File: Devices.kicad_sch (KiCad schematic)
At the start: 0 parts

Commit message: USB and PWR sch
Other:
- title: (none) -> Devices
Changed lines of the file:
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@@
 	(generator_version "8.0")
 	(paper "A4")
+	(title_block
+		(title "Devices")
+	)
 	(sheet
 		(at 20.32 39.37)

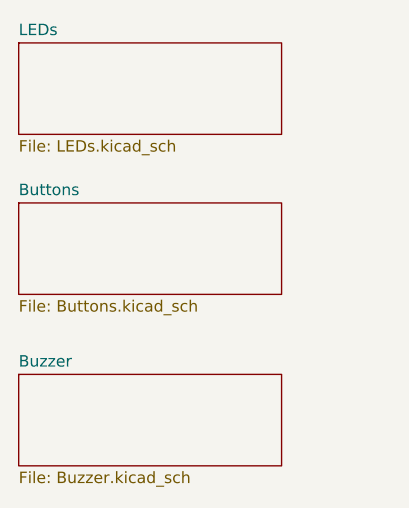
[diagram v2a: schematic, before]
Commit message: add BOOT/RST switches
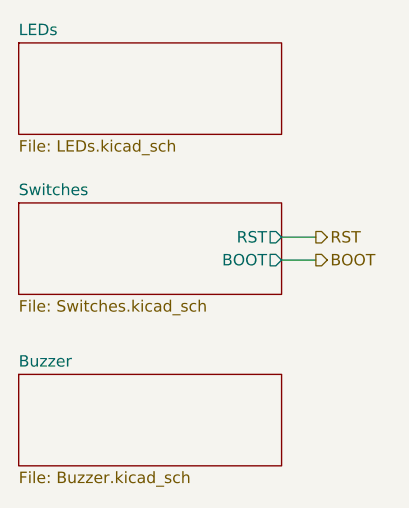
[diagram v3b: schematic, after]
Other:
- sheet Buttons renamed Switches
- sheet Switches: file Buttons.kicad_sch -> Switches.kicad_sch
- sheet Switches ports: added BOOT, RST; removed none
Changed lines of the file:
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@@
 		(title "Devices")
+	)
+	(wire
+		(pts
+			(xy 49.53 43.18) (xy 53.34 43.18)
+		)
+		(stroke
+			(width 0)
+			(type default)
+		)
+	)
+	(wire
+		(pts
+			(xy 49.53 45.72) (xy 53.34 45.72)
+		)
+		(stroke
+			(width 0)
+			(type default)
+		)
+	)
+	(hierarchical_label "RST"
+		(shape output)
+		(at 53.34 43.18 0)
+		(fields_autoplaced yes)
+		(effects
+			(font
+				(size 1.27 1.27)
+			)
+			(justify left)
+		)
+	)
+	(hierarchical_label "BOOT"
+		(shape output)
+		(at 53.34 45.72 0)
+		(fields_autoplaced yes)
+		(effects
+			(font
+				(size 1.27 1.27)
+			)
+			(justify left)
+		)
 	)
 	(sheet
@@
 			(color 0 0 0 0.0000)
 		)
-		(property "Sheetname" "Buttons"
+		(property "Sheetname" "Switches"
 			(at 20.32 38.6584 0)
 			(effects
@@
 			)
 		)
-		(property "Sheetfile" "Buttons.kicad_sch"
+		(property "Sheetfile" "Switches.kicad_sch"
 			(at 20.32 50.1146 0)
 			(effects
@@
 			)
 		)
+		(pin "RST" output
+			(at 49.53 43.18 0)
+			(effects
+				(font
+					(size 1.27 1.27)
+				)
+				(justify right)
+			)
+		)
+		(pin "BOOT" output
+			(at 49.53 45.72 0)
+			(effects
+				(font
+					(size 1.27 1.27)
+				)
+				(justify right)
+			)
+		)

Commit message: finished sch? (need P/Ns)
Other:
- removed sheet Buzzer
- sheet LEDs ports: added LED_0; removed none
- sheet Switches ports: added FLIP, FLOP; removed none
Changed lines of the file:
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@@
+	(wire
+		(pts
+			(xy 49.53 48.26) (xy 53.34 48.26)
+		)
+		(stroke
+			(width 0)
+			(type default)
+		)
+	)
+	(wire
+		(pts
+			(xy 49.53 26.67) (xy 53.34 26.67)
+		)
+		(stroke
+			(width 0)
+			(type default)
+		)
+	)
 	(wire
 		(pts
@@
 	(wire
 		(pts
+			(xy 49.53 50.8) (xy 53.34 50.8)
+		)
+		(stroke
+			(width 0)
+			(type default)
+		)
+	)
+	(wire
+		(pts
 			(xy 49.53 45.72) (xy 53.34 45.72)
 		)
@@
 		)
 	)
+	(hierarchical_label "FLIP"
+		(shape output)
+		(at 53.34 48.26 0)
+		(fields_autoplaced yes)
+		(effects
+			(font
+				(size 1.27 1.27)
+			)
+			(justify left)
+		)
+	)
+	(hierarchical_label "FLOP"
+		(shape output)
+		(at 53.34 50.8 0)
+		(fields_autoplaced yes)
+		(effects
+			(font
+				(size 1.27 1.27)
+			)
+			(justify left)
+		)
+	)
 	(hierarchical_label "BOOT"
 		(shape output)
 		(at 53.34 45.72 0)
+		(fields_autoplaced yes)
+		(effects
+			(font
+				(size 1.27 1.27)
+			)
+			(justify left)
+		)
+	)
+	(hierarchical_label "LED_0"
+		(shape input)
+		(at 53.34 26.67 0)
 		(fields_autoplaced yes)
 		(effects
@@
 	(sheet
 		(at 20.32 39.37)
-		(size 29.21 10.16)
+		(size 29.21 15.24)
 		(fields_autoplaced yes)
 		(stroke
@@
 		)
 		(property "Sheetfile" "Switches.kicad_sch"
-			(at 20.32 50.1146 0)
+			(at 20.32 55.1946 0)
 			(effects
 				(font
@@
 		(pin "BOOT" output
 			(at 49.53 45.72 0)
+			(effects
+				(font
+					(size 1.27 1.27)
+				)
+				(justify right)
+			)
+		)
+		(pin "FLIP" output
+			(at 49.53 48.26 0)
+			(effects
+				(font
+					(size 1.27 1.27)
+				)
+				(justify right)
+			)
+		)
+		(pin "FLOP" output
+			(at 49.53 50.8 0)
 			(effects
 				(font
@@
 	)
 	(sheet
-		(at 20.32 58.42)
+		(at 20.32 21.59)
 		(size 29.21 10.16)
 		(fields_autoplaced yes)
@@
 			(color 0 0 0 0.0000)
 		)
-		(property "Sheetname" "Buzzer"
-			(at 20.32 57.7084 0)
-			(effects
-				(font
-					(size 1.27 1.27)
-				)
-				(justify left bottom)
-			)
-		)
-		(property "Sheetfile" "Buzzer.kicad_sch"
-			(at 20.32 69.1646 0)
-			(effects
-				(font
-					(size 1.27 1.27)
-				)
-				(justify left top)
-			)
-		)
-		(instances
-			(project "esp32-devboard"
-				(path "/0204cec0-d71e-48a7-8736-ccb0d3e9b02c/d1e7b685-9c83-4c15-8db3-0beed5698ce7"
-					(page "5")
-				)
-			)
-		)
-	)
-	(sheet
-		(at 20.32 21.59)
-		(size 29.21 10.16)
-		(fields_autoplaced yes)
-		(stroke
-			(width 0.1524)
-			(type solid)
-		)
-		(fill
-			(color 0 0 0 0.0000)
-		)
 		(property "Sheetname" "LEDs"
 			(at 20.32 20.8784 0)
@@
 			)
 		)
+		(pin "LED_0" input
+			(at 49.53 26.67 0)
+			(effects
+				(font
+					(size 1.27 1.27)
+				)
+				(justify right)
+			)
+		)
